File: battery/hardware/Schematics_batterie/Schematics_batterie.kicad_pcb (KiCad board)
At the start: 2 copper layers, 26 parts, among them IC1 BQ25185DLHR, J1 USB_C_Receptacle_USB2.0_16P, J3 Conn_01x02, J4 Conn_ST_STDC14, U1 BU33SD5WG-TR, U2 STM32G431KBTx, U3 USBLC6-2SC6

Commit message: mise en place des étiquettes
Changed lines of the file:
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@@
 		)
 		(property "Arrow Part Number" ""
-			(at 0 0 0)
+			(at 0.01 0.14 0)
 			(unlocked yes)
 			(layer "F.Fab")
@@
 		)
 		(property "Arrow Price/Stock" ""
-			(at 0 0 0)
+			(at 0.01 0.14 0)
 			(unlocked yes)
 			(layer "F.Fab")
@@
 		(fp_line
 			(start -1.25 -1.385)
-			(end 1.25 -1.385)
+			(end 1.025 -1.385)
 			(stroke
 				(width 0.12)
@@
 		)
 		(fp_line
-			(start -1.25 1.385)
-			(end 1.25 1.385)
+			(start -1.25 1.125)
+			(end 1.05 1.125)
 			(stroke
 				(width 0.12)
@@
 		)
 		(fp_line
-			(start -1.25 -0.625)
-			(end -0.625 -1.25)
-			(stroke
-				(width 0.1)
-				(type solid)
-			)
-			(layer "F.Fab")
-		)
-		(fp_line
-			(start -1.25 1.25)
-			(end -1.25 -0.625)
-			(stroke
-				(width 0.1)
-				(type solid)
-			)
-			(layer "F.Fab")
-		)
-		(fp_line
-			(start -0.625 -1.25)
-			(end 1.25 -1.25)
-			(stroke
-				(width 0.1)
-				(type solid)
-			)
-			(layer "F.Fab")
-		)
-		(fp_line
-			(start 1.25 -1.25)
-			(end 1.25 1.25)
-			(stroke
-				(width 0.1)
-				(type solid)
-			)
-			(layer "F.Fab")
-		)
-		(fp_line
-			(start 1.25 1.25)
-			(end -1.25 1.25)
+			(start -1.275 -0.775)
+			(end -0.85 -1.25)
+			(stroke
+				(width 0.1)
+				(type solid)
+			)
+			(layer "F.Fab")
+		)
+		(fp_line
+			(start -1.275 0.875)
+			(end -1.275 -0.775)
+			(stroke
+				(width 0.1)
+				(type solid)
+			)
+			(layer "F.Fab")
+		)
+		(fp_line
+			(start -0.85 -1.25)
+			(end 1.025 -1.25)
+			(stroke
+				(width 0.1)
+				(type solid)
+			)
+			(layer "F.Fab")
+		)
+		(fp_line
+			(start 1.025 -1.25)
+			(end 1.025 0.9)
+			(stroke
+				(width 0.1)
+				(type solid)
+			)
+			(layer "F.Fab")
+		)
+		(fp_line
+			(start 1.025 0.9)
+			(end -1.275 0.9)
 			(stroke
 				(width 0.1)
@@
 		)
 		(pad "" smd roundrect
-			(at -0.3 -0.5)
-			(size 0.48 0.81)
-			(layers "F.Paste")
-			(roundrect_rratio 0.25)
-		)
-		(pad "" smd roundrect
-			(at -0.3 0.5)
-			(size 0.48 0.81)
-			(layers "F.Paste")
-			(roundrect_rratio 0.25)
-		)
-		(pad "" smd roundrect
-			(at 0.3 -0.5)
-			(size 0.48 0.81)
-			(layers "F.Paste")
-			(roundrect_rratio 0.25)
-		)
-		(pad "" smd roundrect
-			(at 0.3 0.5)
-			(size 0.48 0.81)
+			(at -0.35 -0.52)
+			(size 0.33 0.545)
+			(layers "F.Paste")
+			(roundrect_rratio 0.25)
+		)
+		(pad "" smd roundrect
+			(at -0.35 0.08)
+			(size 0.33 0.545)
+			(layers "F.Paste")
+			(roundrect_rratio 0.25)
+		)
+		(pad "" smd roundrect
+			(at 0.04 -0.52)
+			(size 0.33 0.545)
+			(layers "F.Paste")
+			(roundrect_rratio 0.25)
+		)
+		(pad "" smd roundrect
+			(at 0.05 0.07)
+			(size 0.33 0.545)
 			(layers "F.Paste")
 			(roundrect_rratio 0.25)
@@
 		)
 		(pad "2" smd roundrect
-			(at -1.2125 -0.5)
+			(at -1.2125 -0.6)
 			(size 0.825 0.25)
 			(layers "F.Cu" "F.Paste" "F.Mask")
@@
 		)
 		(pad "3" smd roundrect
-			(at -1.2125 0)
+			(at -1.2125 -0.2)
 			(size 0.825 0.25)
 			(layers "F.Cu" "F.Paste" "F.Mask")
@@
 		)
 		(pad "4" smd roundrect
-			(at -1.2125 0.5)
+			(at -1.2125 0.2)
 			(size 0.825 0.25)
 			(layers "F.Cu" "F.Paste" "F.Mask")
@@
 		)
 		(pad "5" smd roundrect
-			(at -1.2125 1)
+			(at -1.2125 0.6)
 			(size 0.825 0.25)
 			(layers "F.Cu" "F.Paste" "F.Mask")
@@
 		)
 		(pad "6" smd roundrect
-			(at 1.2125 1)
+			(at 0.9 0.6)
 			(size 0.825 0.25)
 			(layers "F.Cu" "F.Paste" "F.Mask")
@@
 		)
 		(pad "7" smd roundrect
-			(at 1.2125 0.5)
+			(at 0.9 0.2)
 			(size 0.825 0.25)
 			(layers "F.Cu" "F.Paste" "F.Mask")
@@
 		)
 		(pad "8" smd roundrect
-			(at 1.2125 0)
+			(at 0.9 -0.2)
 			(size 0.825 0.25)
 			(layers "F.Cu" "F.Paste" "F.Mask")
@@
 		)
 		(pad "9" smd roundrect
-			(at 1.2125 -0.5)
+			(at 0.9 -0.6)
 			(size 0.825 0.25)
 			(layers "F.Cu" "F.Paste" "F.Mask")
@@
 		)
 		(pad "10" smd roundrect
-			(at 1.2125 -1)
+			(at 0.9 -1)
 			(size 0.825 0.25)
 			(layers "F.Cu" "F.Paste" "F.Mask")
@@
 		)
 		(pad "11" smd rect
-			(at 0 0)
-			(size 1.2 2)
+			(at -0.14 -0.22)
+			(size 0.85 1.38)
 			(property pad_prop_heatsink)
 			(layers "F.Cu" "F.Mask")

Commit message: Début du PCB
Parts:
- added D2: Green_LED, LED_SMD:LED_0603_1608Metric_Pad1.05x0.95mm_HandSolder, F.Cu at (128.2, 59.4)
- added H1: MountingHole_Pad, MountingHole:MountingHole_3.2mm_M3_Pad_Via, F.Cu at (145.0, 50.0)
- added H2: MountingHole_Pad, MountingHole:MountingHole_3.2mm_M3_Pad_Via, F.Cu at (110.0, 50.0)
- added H3: MountingHole_Pad, MountingHole:MountingHole_3.2mm_M3_Pad_Via, F.Cu at (145.0, 85.0)
- added H4: MountingHole_Pad, MountingHole:MountingHole_3.2mm_M3_Pad_Via, F.Cu at (110.0, 85.0)
- added J2: Conn_01x02, Connector_JST:JST_XH_B2B-XH-A_1x02_P2.50mm_Vertical, F.Cu at (146.1, 78.6)
- added J5: Conn_01x02, Connector_JST:JST_XH_B2B-XH-A_1x02_P2.50mm_Vertical, F.Cu at (146.0, 70.0)
- added JP2: SolderJumper_2_Open, Jumper:SolderJumper-2_P1.3mm_Open_TrianglePad1.0x1.5mm, F.Cu at (133.5, 80.8)
- added R7: 1k, Resistor_SMD:R_0603_1608Metric_Pad0.98x0.95mm_HandSolder, F.Cu at (131.9, 59.3)
- added TP1: TestPoint, TestPoint:TestPoint_Pad_D2.0mm, F.Cu at (137.1, 58.0)
- added TP2: TestPoint, TestPoint:TestPoint_Pad_D2.0mm, F.Cu at (140.3, 57.9)
- added TP3: TestPoint, TestPoint:TestPoint_Pad_D2.0mm, F.Cu at (137.2, 61.3)
- added TP4: TestPoint, TestPoint:TestPoint_Pad_D2.0mm, F.Cu at (130.2, 72.0)
- added TP5: TestPoint, TestPoint:TestPoint_Pad_D2.0mm, F.Cu at (140.2, 61.3)
- added TP6: TestPoint, TestPoint:TestPoint_Pad_D2.0mm, F.Cu at (133.7, 75.7)
- added TP7: TestPoint, TestPoint:TestPoint_Pad_D2.0mm, F.Cu at (138.6, 75.3)
- added TP8: TestPoint, TestPoint:TestPoint_Pad_D2.0mm, F.Cu at (138.7, 72.2)
- C1, C11, C2, C3, C4, C5, C6, C7: footprint Capacitor_SMD:C_0603_1608Metric_Pad1.08x0.95mm_HandSolder -> Capacitor_SMD:C_0603_1608Metric
- C10, C8, C9: footprint Capacitor_SMD:C_0603_1608Metric_Pad1.08x0.95mm_HandSolder -> Capacitor_SMD:C_0402_1005Metric
- R1: value 100 k -> 1k
- moved J1 55.4 mm to (123.5, 49.2), turned to 180 degrees
- moved D1 54.8 mm to (128.2, 60.9), turned to 180 degrees
- moved R2 47.5 mm to (130.5, 50.3)
- moved U3 45.8 mm to (123.5, 57.4), turned to -90 degrees
- moved J3 43.7 mm to (146.0, 61.6), turned to 90 degrees
- moved R4 43.7 mm to (116.5, 50.1)
- moved J4 43.6 mm to (112.2, 65.0)
- moved IC1 41.7 mm to (134.4, 69.6)
- moved U2 39.1 mm to (123.0, 68.0), turned to 90 degrees
- moved R1 34.4 mm to (131.9, 60.9)
- moved U1 31.6 mm to (126.2, 80.0), turned to 180 degrees
- moved L1 31.4 mm to (128.2, 62.5), turned to 180 degrees
- moved C6 30.2 mm to (129.2, 64.8), turned to 90 degrees
- moved C1 30.2 mm to (119.4, 56.0)
- moved C7 29.5 mm to (118.1, 72.5), turned to 180 degrees
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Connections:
- net Net-(D1-K) renamed /LED_Stat
- net Net-(IC1-ILIM/VSET) renamed /Ilim/Vset
- net Net-(IC1-ISET) renamed /Iset
- net Net-(IC1-TS/MR) renamed /TS MR
- C1 pad 1: +5V -> GND
- C1 pad 2: GND -> +5V
- C4 pad 1: +5V -> /VIN
- J3 pad 1: +5V -> BAT
- U1 pad 1: +5V -> /VIN
- U1 pad 3: +5V -> /VIN
- U2 pad 10: unconnected-(U2-PA5-Pad10) -> STAT1
- U2 pad 11: unconnected-(U2-PA6-Pad11) -> STAT2
- U2 pad 12: LED_Status -> SYS
- U2 pad 18: unconnected-(U2-PA8-Pad18) -> LED_Status
- U2 pad 19: unconnected-(U2-PA9-Pad19) -> LED_Playing
- U2 pad 9: unconnected-(U2-PA4-Pad9) -> Charge Enabler
- U3 pad 1: D_p_1 -> D_m_1
- U3 pad 3: D_m_1 -> D_p_1
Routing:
- net BAT: track 0.00 -> 56.6 mm, vias 0 -> 2
- net +5V: track 0.00 -> 35.4 mm, vias 0 -> 3
- net GND: track 0.00 -> 34.6 mm, vias 0 -> 23
- net STAT1: track 0.00 -> 30.4 mm, vias 0 -> 3
- net USART2_RX: track 0.00 -> 26.1 mm
- net STAT2: track 0.00 -> 22.3 mm, vias 0 -> 2
- net USART2_TX: track 0.00 -> 21.5 mm
- net SYS: track 0.00 -> 19.1 mm
- net NRST: track 0.00 -> 17.9 mm
- net +3.3V: track 0.00 -> 9.19 mm, vias 0 -> 1
- net Charge Enabler: track 0.00 -> 8.77 mm
- net /VIN: track 0.00 -> 8.32 mm
- net +3.3VA: track 0.00 -> 8.28 mm
- net SYS_SWDIO: track 0.00 -> 8.04 mm
- net /Ilim/Vset: track 0.00 -> 7.15 mm
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- added copper zone on B.Cu, net GND
- added copper zone on F.Cu, net GND
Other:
- board outline added: 45 x 45 mm

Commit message: derniers branchements et isolation des textes
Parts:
- moved U2 0.08 mm to (123.0, 67.9)
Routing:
- net +3.3V: track 9.19 -> 46.8 mm, vias 1 -> 3

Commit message: plus que 2 erreurs à régler lundi avec le professeur, sinon le pcb est terminé
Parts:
- moved D2 0.15 mm to (128.2, 59.2)
- moved R7 0.10 mm to (131.9, 59.2)
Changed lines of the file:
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@@
 	)
 	(setup
+		(stackup
+			(layer "F.SilkS"
+				(type "Top Silk Screen")
+			)
+			(layer "F.Paste"
+				(type "Top Solder Paste")
+			)
+			(layer "F.Mask"
+				(type "Top Solder Mask")
+				(thickness 0.01)
+			)
+			(layer "F.Cu"
+				(type "copper")
+				(thickness 0.035)
+			)
+			(layer "dielectric 1"
+				(type "core")
+				(thickness 1.51)
+				(material "FR4")
+				(epsilon_r 4.5)
+				(loss_tangent 0.02)
+			)
+			(layer "B.Cu"
+				(type "copper")
+				(thickness 0.035)
+			)
+			(layer "B.Mask"
+				(type "Bottom Solder Mask")
+				(thickness 0.01)
+			)
+			(layer "B.Paste"
+				(type "Bottom Solder Paste")
+			)
+			(layer "B.SilkS"
+				(type "Bottom Silk Screen")
+			)
+			(copper_finish "None")
+			(dielectric_constraints no)
+		)
 		(pad_to_mask_clearance 0)
 		(allow_soldermask_bridges_in_footprints no)
@@
 	(footprint "LED_SMD:LED_0603_1608Metric_Pad1.05x0.95mm_HandSolder"
 		(layer "F.Cu")
-		(at 128.25 59.35 180)
+		(at 128.25 59.2 180)
 		(descr "LED SMD 0603 (1608 Metric), square (rectangular) end terminal, IPC_7351 nominal, (Body size source: http://www.tortai-tech.com/upload/download/2011102023233369053.pdf), generated with kicad-footprint-generator")
 		(tags "LED handsolder")
@@
 		(tags "inductor handsolder")
 		(property "Reference" "L1"
-			(at 0.05 4.6 0)
+			(at 0.05 4.7 0)
 			(layer "F.SilkS")
 			(effects
@@
 		(tags "SOT TO_SOT_SMD")
 		(property "Reference" "U3"
-			(at 0 -2.4 90)
+			(at -0.1625 -3.2 90)
 			(layer "F.SilkS")
 			(effects
@@
 	(footprint "Resistor_SMD:R_0603_1608Metric_Pad0.98x0.95mm_HandSolder"
 		(layer "F.Cu")
-		(at 131.9 59.3)
+		(at 131.9 59.2)
 		(descr "Resistor SMD 0603 (1608 Metric), square (rectangular) end terminal, IPC_7351 nominal with elongated pad for handsoldering. (Body size source: IPC-SM-782 page 72, https://www.pcb-3d.com/wordpress/wp-content/uploads/ipc-sm-782a_amendment_1_and_2.pdf), generated with kicad-footprint-generator")
 		(tags "resistor handsolder")
@@
 	)
 	(segment
-		(start 132.8125 59.3)
-		(end 133.95 59.3)
+		(start 120.3 52.92)
+		(end 120.3 54.025)
 		(width 0.4)
 		(layer "F.Cu")
@@
 	)
 	(segment
-		(start 120.3 52.92)
-		(end 120.3 54.025)
+		(start 132.8125 59.3)
+		(end 133.95 59.3)
 		(width 0.4)
 		(layer "F.Cu")
@@
 	)
 	(segment
-		(start 124.2 62.525)
+		(start 127.225 59.35)
 		(end 127.375 59.35)
 		(width 0.3)
@@
 	(segment
 		(start 124.2 63.825)
-		(end 124.2 62.525)
+		(end 124.2 62.375)
+		(width 0.3)
+		(layer "F.Cu")
+		(net 39)
+	)
+	(segment
+		(start 124.2 62.375)
+		(end 127.225 59.35)
 		(width 0.3)
 		(layer "F.Cu")

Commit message: FIN DU PCCCBBBBBB
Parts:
- added C12: 100nF, Capacitor_SMD:C_0402_1005Metric, F.Cu at (129.5, 75.0)
- added R8: 9k, Resistor_SMD:R_0603_1608Metric, F.Cu at (133.7, 78.2)
- added R9: 1k, Resistor_SMD:R_0603_1608Metric, F.Cu at (130.8, 75.2)
- D1, D2: footprint LED_SMD:LED_0603_1608Metric_Pad1.05x0.95mm_HandSolder -> LED_SMD:LED_0603_1608Metric
- L1: footprint Inductor_SMD:L_0603_1608Metric_Pad1.05x0.95mm_HandSolder -> Inductor_SMD:L_0603_1608Metric
- R1, R2, R3, R4, R5, R6, R7: footprint Resistor_SMD:R_0603_1608Metric_Pad0.98x0.95mm_HandSolder -> Resistor_SMD:R_0603_1608Metric
- moved TP2 22.9 mm to (140.2, 80.8)
- moved C7 0.62 mm to (117.5, 72.5)
- moved C2 0.23 mm to (130.7, 67.8)
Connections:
- J3 pad 1: BAT -> SYS
- J5 pad 1: BAT -> SYS
- U2 pad 5: unconnected-(U2-PA0-Pad5) -> VBAT
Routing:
- net BAT: track 56.6 -> 40.3 mm, vias 2 -> 0
- net VBAT: track 0.00 -> 13.2 mm, vias 0 -> 2
- net SYS: track 19.1 -> 12.3 mm, vias 0 -> 3
- net GND: track 34.6 -> 38.9 mm, vias 23 -> 25
- net NRST: track 17.9 -> 19.6 mm
- net +5V: track 35.4 -> 34.0 mm
- net STAT1: track 30.4 -> 31.5 mm
- net +3.3V: track 46.8 -> 47.8 mm
- added copper zone on F.Cu, net +5V
- added copper zone on F.Cu, net BAT
- added copper zone on F.Cu, net SYS
- removed copper zone on F.Cu, net GND

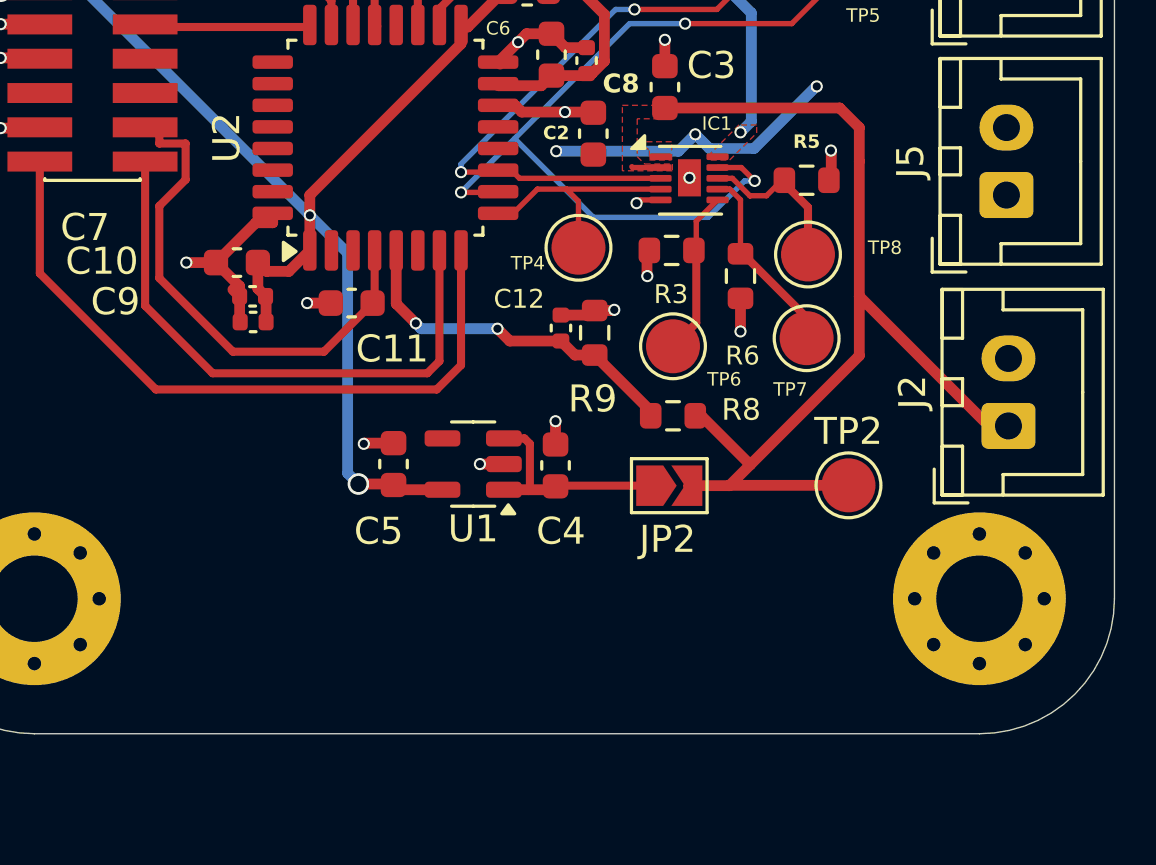
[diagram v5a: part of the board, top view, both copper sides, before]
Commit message: il manque encore les gerbers
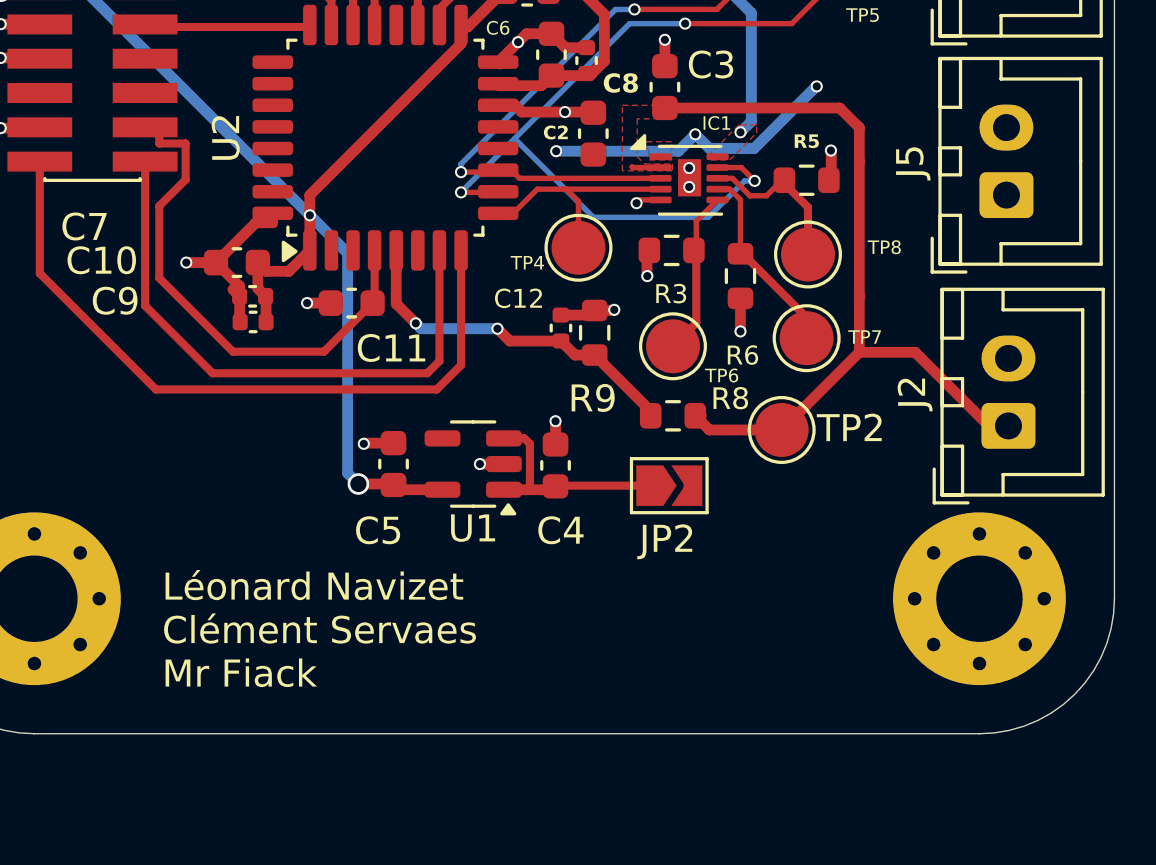
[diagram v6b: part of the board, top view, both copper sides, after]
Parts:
- moved TP2 3.21 mm to (137.7, 78.8)
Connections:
- JP2 pad 2: BAT -> SYS
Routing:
- net BAT: track 40.3 -> 31.3 mm
- net GND: vias 25 -> 26
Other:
- board text added: "Léonard Navizet Clément Servaes Mr Fiack"
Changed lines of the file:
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@@
 		)
 		(pad_to_mask_clearance 0)
+		(pad_to_paste_clearance_ratio -0.15)
 		(allow_soldermask_bridges_in_footprints no)
 		(pcbplotparams
@@
 			(usegerberattributes yes)
 			(usegerberadvancedattributes yes)
-			(creategerberjobfile yes)
+			(creategerberjobfile no)
 			(dashed_line_dash_ratio 12.000000)
 			(dashed_line_gap_ratio 3.000000)
@@
 			(outputformat 1)
 			(mirror no)
-			(drillshape 1)
+			(drillshape 0)
 			(scaleselection 1)
-			(outputdirectory "")
+			(outputdirectory "../gerber/")
 		)
 	)
@@
 	(footprint "TestPoint:TestPoint_Pad_D2.0mm"
 		(layer "F.Cu")
-		(at 140.15 80.8)
+		(at 137.675 78.75)
 		(descr "SMD pad as test Point, diameter 2.0mm")
 		(tags "test point SMD pad")
 		(property "Reference" "TP2"
-			(at 0 -1.998 0)
+			(at 2.575 -0.05 0)
 			(layer "F.SilkS")
 			(effects
@@
 			(size 0.3 0.3)
 			(layers "F.Cu" "F.Mask")
-			(net 4 "BAT")
+			(net 3 "SYS")
 			(pinfunction "B")
 			(pintype "passive")
@@
 		(tags "test point SMD pad")
 		(property "Reference" "TP6"
-			(at 1.9 1.225 0)
+			(at 1.825 1.1 0)
 			(layer "F.SilkS")
 			(effects
@@
 		(tags "resistor")
 		(property "Reference" "R8"
-			(at -2.525 0.225 0)
+			(at -2.125 0.625 0)
 			(layer "F.SilkS")
 			(effects
@@
 		)
 		(property "Value" "9k"
-			(at 0 1.43 360)
+			(at 0 1.43 0)
 			(layer "F.Fab")
 			(effects
@@
 		)
 		(fp_text user "${REFERENCE}"
-			(at 0 0 360)
+			(at 0 0 0)
 			(layer "F.Fab")
 			(effects
@@
 		(tags "test point SMD pad")
 		(property "Reference" "TP7"
-			(at -0.6 1.9 0)
+			(at 2.175 -0.025 0)
 			(layer "F.SilkS")
 			(effects
@@
 		(layer "Edge.Cuts")
 	)
+	(gr_text "Léonard Navizet\nClément Servaes\nMr Fiack\n"
+		(at 114.725 88.375 0)
+		(layer "F.SilkS")
+		(effects
+			(font
+				(size 1 1)
+				(thickness 0.15)
+			)
+			(justify left bottom)
+		)
+	)
 	(segment
 		(start 125.85 54.8625)
@@
 	)
 	(via
+		(at 134.25 69.75)
+		(size 0.45)
+		(drill 0.3)
+		(layers "F.Cu" "B.Cu")
+		(net 2)
+	)
+	(via
 		(at 108.75 67.57)
 		(size 0.45)
@@
 	)
 	(via
-		(at 134.26 69.41)
+		(at 134.25 69.05)
 		(size 0.45)
 		(drill 0.3)
@@
 	)
 	(segment
+		(start 134.2375 80.8125)
+		(end 134.2375 81.0875)
+		(width 0.4)
+		(layer "F.Cu")
+		(net 3)
+	)
+	(segment
 		(start 137.05 58.05)
 		(end 137.05 58.75)
@@
 	)
 	(segment
-		(start 134.2375 80.8125)
-		(end 134.2375 81.0875)
-		(width 0.4)
-		(layer "F.Cu")
-		(net 4)
-	)
-	(segment
-		(start 145.35 78.6)
-		(end 140.55 73.8)
+		(start 142.625 75.875)
+		(end 142.85 76.1)
 		(width 0.4)
 		(layer "F.Cu")
@@
 	)
 	(segment
-		(start 135.7375 80.8125)
-		(end 134.2375 80.8125)
+		(start 140.55 68.8)
+		(end 140.55 67.55)
 		(width 0.4)
 		(layer "F.Cu")
@@
 	)
 	(segment
-		(start 140.55 68.8)
-		(end 140.55 67.55)
+		(start 145.35 78.6)
+		(end 142.85 76.1)
 		(width 0.4)
 		(layer "F.Cu")
@@
 	)
 	(segment
-		(start 140.55 76)
-		(end 136.5125 80.0375)
-		(width 0.4)
+		(start 132.155 69.03)
+		(end 132.125 69)
+		(width 0.2)
 		(layer "F.Cu")
 		(net 4)
 	)
 	(segment
-		(start 136.5125 80.0375)
-		(end 135.7375 80.8125)
+		(start 140.55 75.875)
+		(end 137.675 78.75)
 		(width 0.4)
 		(layer "F.Cu")
@@
 	)
 	(segment
-		(start 135.75 80.8)
-		(end 140.15 80.8)
+		(start 140.55 73.8)
+		(end 140.55 75.875)
 		(width 0.4)
 		(layer "F.Cu")
@@
 	)
 	(segment
-		(start 132.155 69.03)
-		(end 132.125 69)
-		(width 0.2)
+		(start 135 78.75)
+		(end 134.475 78.225)
+		(width 0.4)
 		(layer "F.Cu")
 		(net 4)
@@
 	)
 	(segment
-		(start 136.5125 80.0375)
-		(end 134.7 78.225)
+		(start 140.55 75.875)
+		(end 142.625 75.875)
 		(width 0.4)
 		(layer "F.Cu")
@@
 	)
 	(segment
-		(start 135.7375 80.8125)
-		(end 135.75 80.8)
+		(start 137.675 78.75)
+		(end 135 78.75)
 		(width 0.4)
 		(layer "F.Cu")
@@
 		(layer "F.Cu")
 		(net 4)
-	)
-	(segment
-		(start 140.55 73.8)
-		(end 140.55 76)
-		(width 0.4)
-		(layer "F.Cu")
-		(net 4)

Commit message: Gerbers+nokotan
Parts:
- added G***: LOGO, LOGO, F.Cu at (135.6, 86.6)
